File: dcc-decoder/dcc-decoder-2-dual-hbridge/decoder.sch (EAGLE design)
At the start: 30 parts, among them U4 ATMEGA328P, U5 MPC17531-ES, Y1 16MHZ

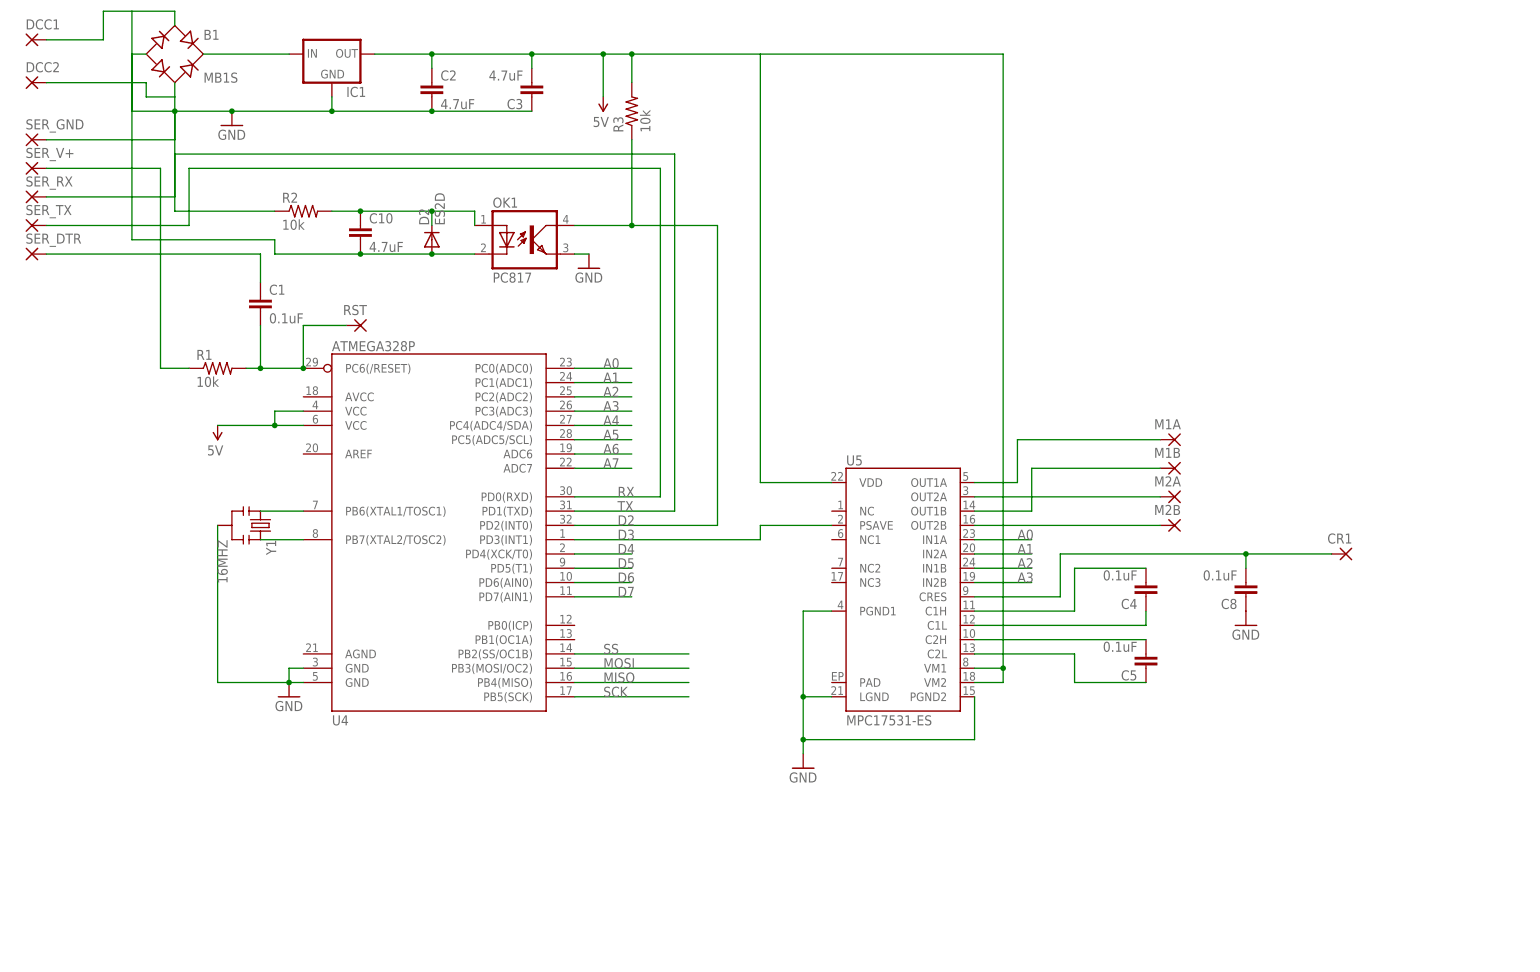
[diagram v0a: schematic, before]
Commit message: New layout for RFM69HC
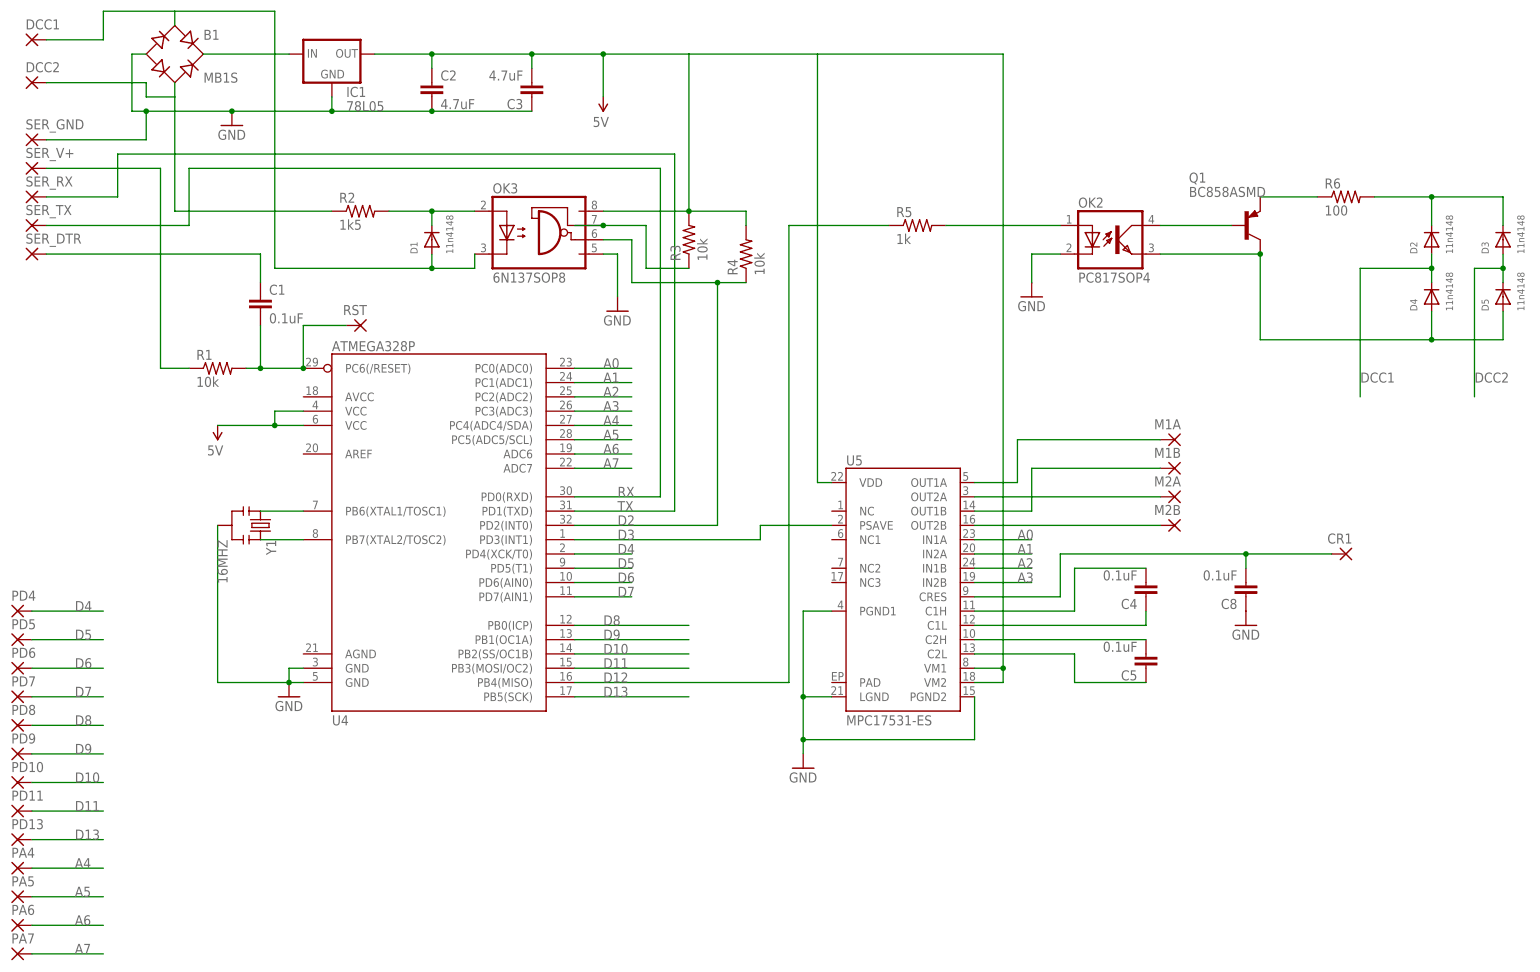
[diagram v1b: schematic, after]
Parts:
- removed C10: 4.7uF, SparkFun-Capacitors:CAP0805
- removed OK1: PC817, optocoupler:PC817
- added D1, D3, D4, D5: 11n4148, adafruit:DIODESOD-123
- added OK2: PC817SOP4, optocoupler:PC817SOP4
- added OK3: 6N137SOP8, optocoupler:6N137SOP8
- added PA4, PA5, PA6, PA7, PD10, PD11, PD13, PD4, PD5, PD6, PD7, PD8, PD9: (no value), wirepad:SMD2
- added Q1: BC858ASMD, transistor-pnp:BC858ASMD
- added R4: 10k, SparkFun-Resistors:RESISTOR0603-RES
- added R5: 1k, SparkFun-Resistors:RESISTOR0603-RES
- added R6: 100, SparkFun-Resistors:RESISTOR0603-RES
- D2: value ES2D -> 11n4148; device diode:ES2D -> adafruit:DIODESOD-123
- IC1: value (none) -> 78L05
- R2: value 10k -> 1k5
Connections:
- removed net MISO: U4.PB4(MISO)
- removed net MOSI: U4.PB3(MOSI/OC2)
- removed net N$11: B1.AC1, C10.2, D2.A, DCC1.P, OK1.C
- removed net N$22: B1.AC2, DCC2.P, R2.1
- removed net SCK: U4.PB5(SCK)
- removed net SS: U4.PB2(SS/OC1B)
- new net D10: PD10.P, U4.PB2(SS/OC1B)
- new net D11: PD11.P, U4.PB3(MOSI/OC2)
- new net D12: R5.1, U4.PB4(MISO)
- new net D13: PD13.P, U4.PB5(SCK)
- new net D8: PD8.P, U4.PB0(ICP)
- new net D9: PD9.P, U4.PB1(OC1A)
- new net DCC1: B1.AC1, D1.A, D2.A, D4.C, DCC1.P, OK3.C
- new net DCC2: B1.AC2, D3.A, D5.C, DCC2.P, R2.1
- new net N$13: OK3.VE, R3.1
- new net N$16: OK2.A, R5.2
- new net N$18: OK2.COL, Q1.B
- new net N$19: D4.A, D5.A, OK2.EMIT, Q1.C
- new net N$21: Q1.E, R6.1
- new net N$24: D2.C, D3.C, R6.2
- net A4: now also PA4.P
- net A5: now also PA5.P
- net A6: now also PA6.P
- net A7: now also PA7.P
- net D2: now also OK3.VO, R4.1; no longer OK1.COL, R3.1
- net D4: now also PD4.P
- net D5: now also PD5.P
- net D6: now also PD6.P
- net D7: now also PD7.P
- net GND: now also OK2.C, OK3.GND; no longer OK1.EMIT
- net N$8: now also D1.C, OK3.A; no longer C10.1, D2.C, OK1.A
- net VCC: now also OK3.VCC, R4.2
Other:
- moved on the sheet: D2, R2, R3
